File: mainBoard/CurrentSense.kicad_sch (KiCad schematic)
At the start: 16 parts, among them J12 1935161, J13 SJ2-35813B-SMT-TR, U10 LMV321

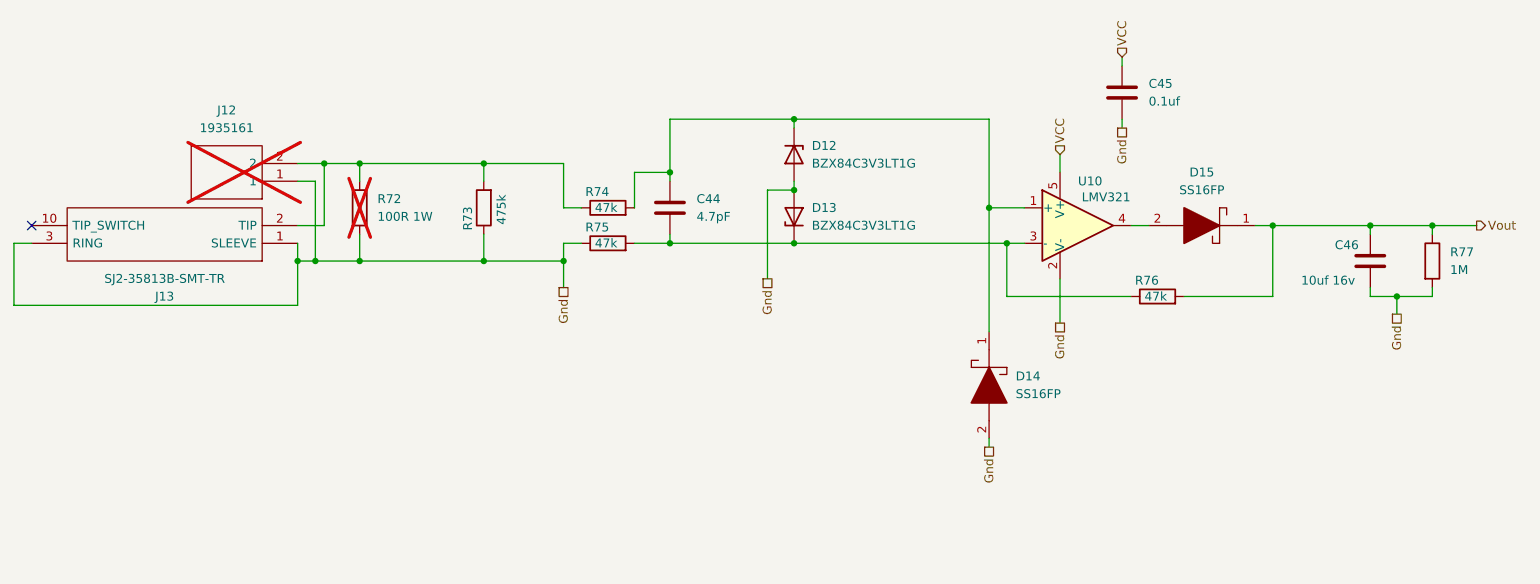
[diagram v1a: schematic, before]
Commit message: add a unit test fixture, and start changing the current measurement circuit
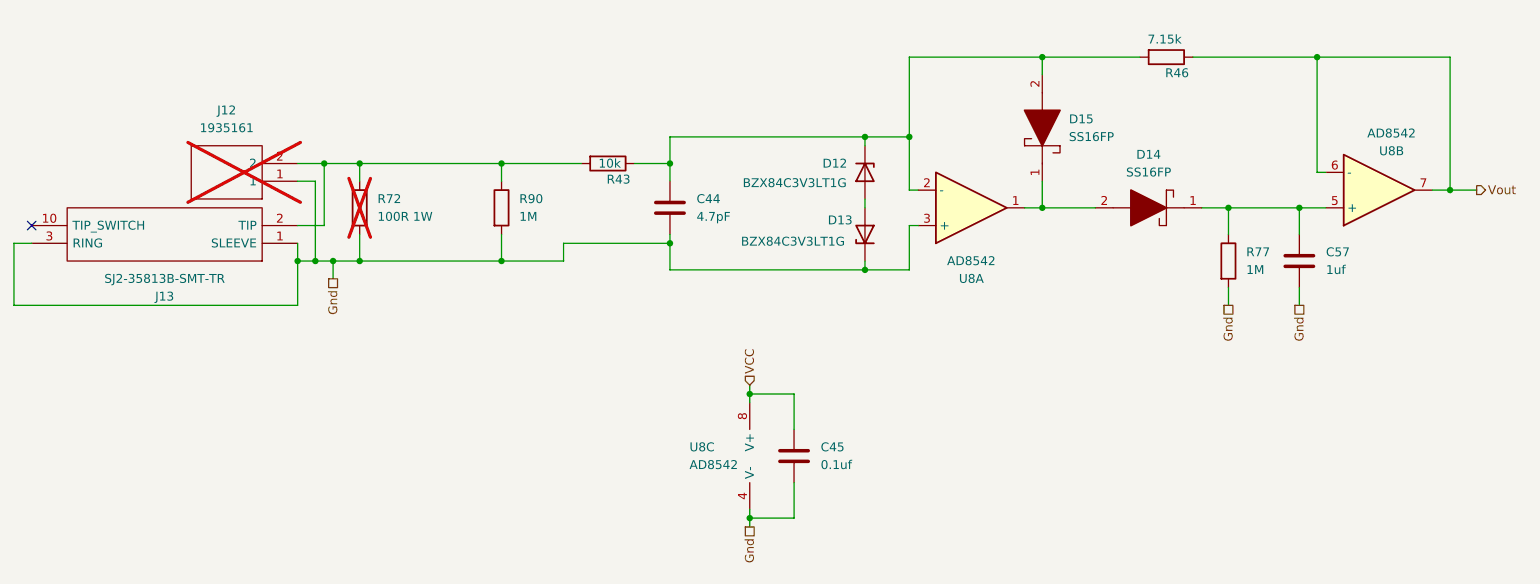
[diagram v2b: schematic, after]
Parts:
- removed C46: 10uf 16v, Capacitor_SMD:C_0805_2012Metric, symbol Device:C
- removed R73: 475k, Resistor_SMD:R_0402_1005Metric, symbol Device:R
- removed R74, R75, R76: 47k, Resistor_SMD:R_0402_1005Metric, symbol Device:R
- removed U10: LMV321, Package_TO_SOT_SMD:SOT-353_SC-70-5, symbol Amplifier_Operational:LMV321
- added C57: 1uf, Capacitor_SMD:C_0805_2012Metric, symbol Device:C
- added R43: 10k, Resistor_SMD:R_0402_1005Metric, symbol Device:R
- added R46: 7.15k, Resistor_SMD:R_0402_1005Metric, symbol Device:R
- added R90: 1M, Resistor_SMD:R_0402_1005Metric, symbol Device:R
- added U8: AD8542, Package_SO:MSOP-8_3x3mm_P0.65mm, symbol Device:Opamp_Dual
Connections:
- net Gnd: now also C44.2, D13.3 (K), C57.2, R90.2, U8.3 (+), U8.4 (V-); no longer D12.1 (A), D13.1 (A), D14.2
- net VCC: now also U8.8 (V+)
- net Vout: now also R46.1, U8.6 (-), U8.7; no longer D15.1, R77.1
- net at J12.2, J13.2 (TIP), R72.1: now also R43.2, R90.1
- net at C44.1, D12.3 (K): now also D15.2, R43.1, R46.2, U8.2 (-); no longer D14.1
- new net: D12.1 (A), D13.1 (A)
- new net: C57.1, D14.1, R77.1, U8.5 (+)
- new net: D14.2, D15.1, U8.1
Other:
- moved on the sheet: C45, D12, D13, D14, D15, R77
